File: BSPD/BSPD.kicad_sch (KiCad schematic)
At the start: 35 parts, among them Q3 PMOS, U1 LM339DR, U10 641964-1, U2 R-78E5.0-0.5, U3 SN74LVC1G08DBVR, U4 SN74LVC3G14DCUR, U5 NE555DR, U6 SN74LVC1G08DBVR, U7 641964-1, U8 SN74AC32DR, U9 641964-1

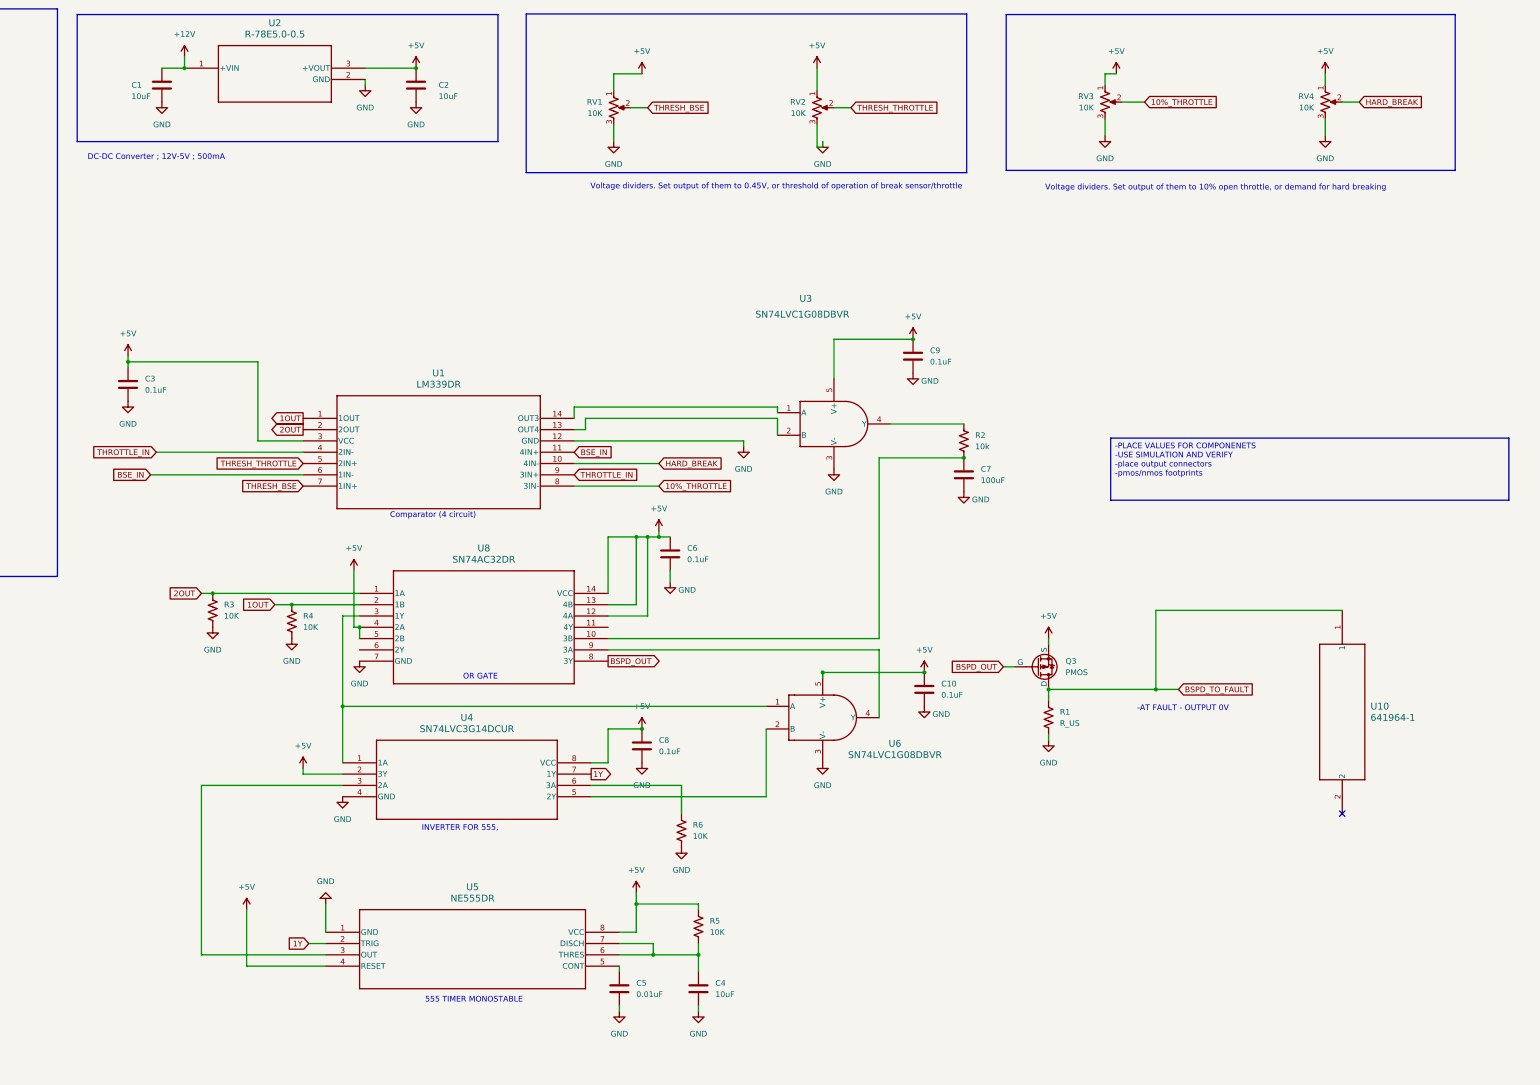
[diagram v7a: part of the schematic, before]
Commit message: Redone logic for BSPD.
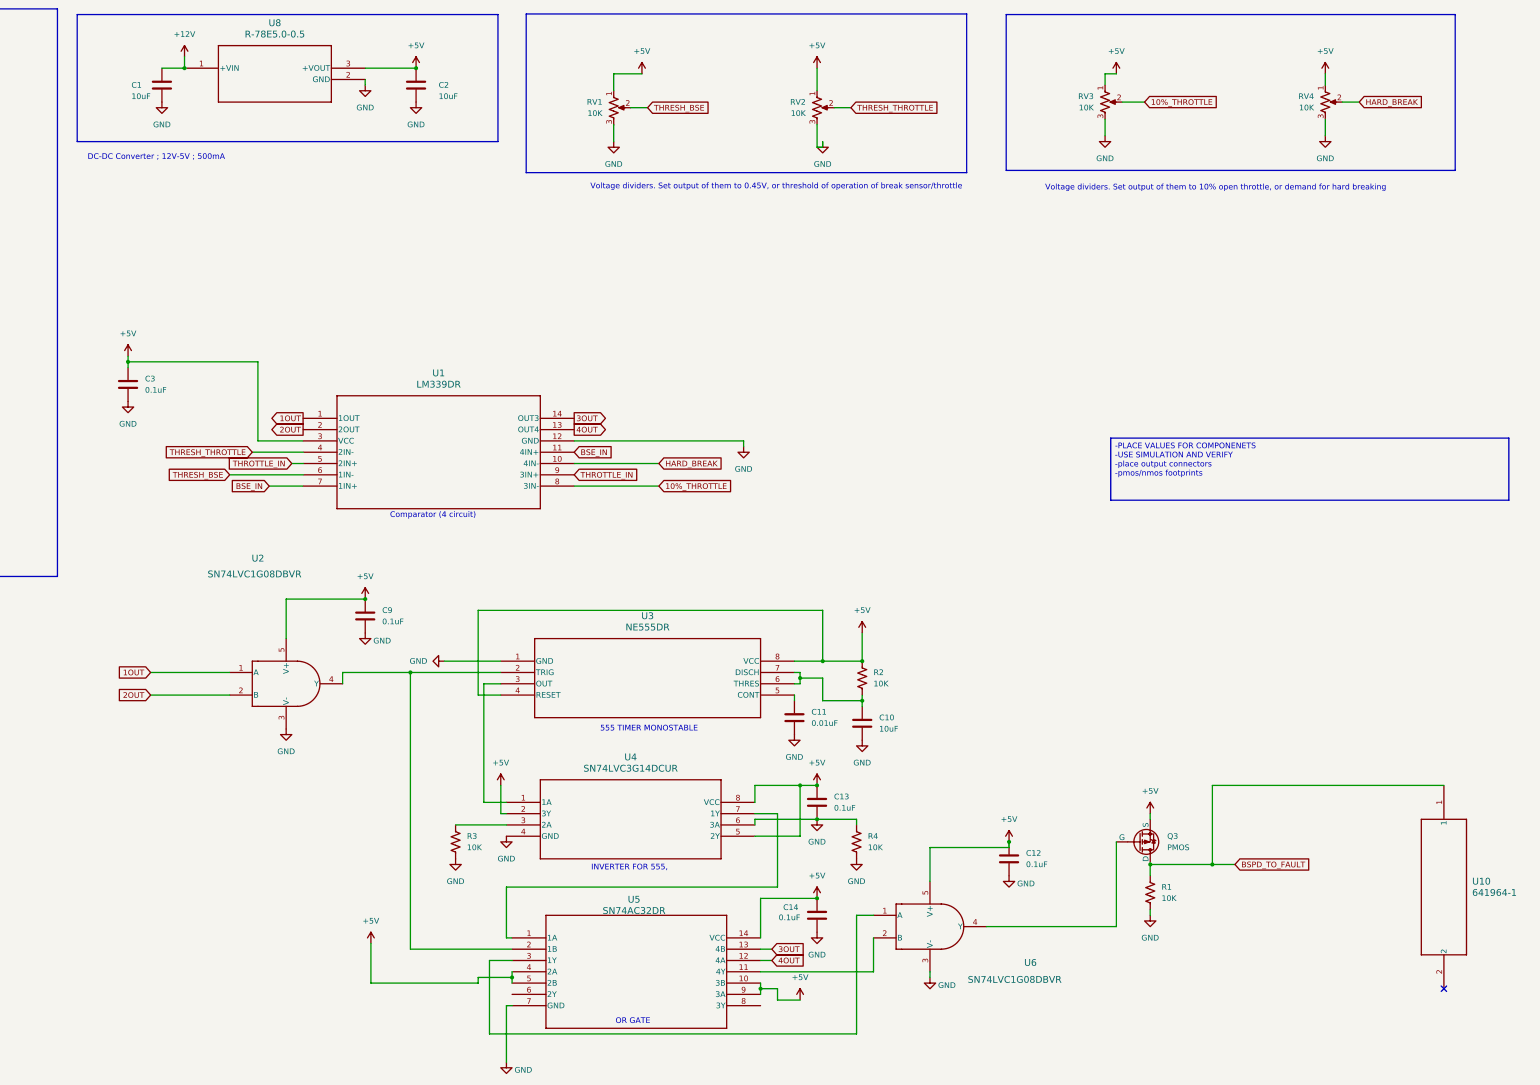
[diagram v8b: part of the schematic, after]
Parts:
- removed C4: 10uF, Capacitor_SMD:C_0805_2012Metric, symbol Device:C
- removed C5: 0.01uF, Capacitor_SMD:C_0805_2012Metric, symbol Device:C
- removed C6, C8: 0.1uF, Capacitor_SMD:C_0805_2012Metric, symbol Device:C
- removed C7: 100uF, Capacitor_SMD:C_1206_3216Metric, symbol Device:C
- removed R5, R6: 10K, Resistor_SMD:R_0402_1005Metric_Pad0.72x0.64mm_HandSolder, symbol Device:R_US
- removed U5: NE555DR, NE555DR:D8, symbol NE555DR:NE555DR
- added C11: 0.01uF, Capacitor_SMD:C_0805_2012Metric, symbol Device:C
- added C12, C13, C14: 0.1uF, Capacitor_SMD:C_0805_2012Metric, symbol Device:C
- added U3: NE555DR, NE555DR:D8, symbol NE555DR:NE555DR
- C10: value 0.1uF -> 10uF
- R1: value R_US -> 10K
- R2: value 10k -> 10K; footprint Resistor_SMD:R_0402_1005Metric_Pad0.72x0.64mm_HandSolder -> Resistor_SMD:R_0805_2012Metric
- R3, R4: footprint Resistor_SMD:R_0402_1005Metric_Pad0.72x0.64mm_HandSolder -> Resistor_SMD:R_0805_2012Metric
- U6: footprint SN74LVC1G08DBVR:DBV0005A_N -> SN74LVC1G08DBVR:DBV0005A_L
- renumbered U3 to U2, U8 to U5, U2 to U8
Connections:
- net +5V: now also R2.1, U4.5 (2Y), U5.10 (3B), U5.9 (3A), C12.1, C13.1, C14.1, U3.4 (RESET), U3.8 (VCC); no longer C10.1, U5.12 (4A), U5.13 (4B)
- net 1OUT: now also U2.1 (A); no longer R4.1, U5.2 (1B)
- net 2OUT: now also U2.2 (B); no longer R3.1, U5.1 (1A)
- net BSE_IN: now also U1.7 (1IN+); no longer U1.6 (1IN-)
- net GND: now also R4.1, U4.6 (3A), C11.2, C12.2, C13.2, C14.2, U3.1 (GND)
- net THRESH_BSE: now also U1.6 (1IN-); no longer U1.7 (1IN+)
- net THRESH_THROTTLE: now also U1.4 (2IN-); no longer U1.5 (2IN+)
- net THROTTLE_IN: now also U1.5 (2IN+); no longer U1.4 (2IN-)
- net at U2.4 (Y): now also U5.2 (1B), U3.2 (TRIG); no longer R2.1
- net at R2.2: now also C10.1, U3.6 (THRES), U3.7 (DISCH); no longer U5.10 (3B)
- net at U4.3 (2A): now also R3.1
- net 4OUT: now reaches U1.13 (OUT4)
- net 4OUT: now also U5.12 (4A); no longer U2.2 (B)
- net 3OUT: now reaches U1.14 (OUT3)
- net 3OUT: now also U5.13 (4B); no longer U2.1 (A)
- net at U5.11 (4Y): now also U6.2 (B)
- net at U5.3 (1Y), U6.1 (A): no longer U4.1 (1A)
- net at U6.4 (Y): now also Q3.2 (G); no longer U5.9 (3A)
- net 1Y: no longer names the net of U4.7 (1Y)
- net 1Y: now also U5.1 (1A)
- net BSPD_OUT: no longer names the net of U5.8 (3Y)
- net BSPD_OUT: no longer Q3.2 (G)
- new net: U3.3 (OUT), U4.1 (1A)
- new net: C11.1, U3.5 (CONT)
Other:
- note removed: "-AT FAULT - OUTPUT 0V"
- moved on the sheet: C9, Q3, R1, U10, U2, U4, U5
